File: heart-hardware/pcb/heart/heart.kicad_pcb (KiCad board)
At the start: 4 copper layers, 49.5 x 44 mm, 62 parts, among them J1 3V0, J2 DIO, J3 CLK, J4 GND, SW1 , U1 STM32L031F6Px, U2 TCA6416APWR, U3 LIS3DH

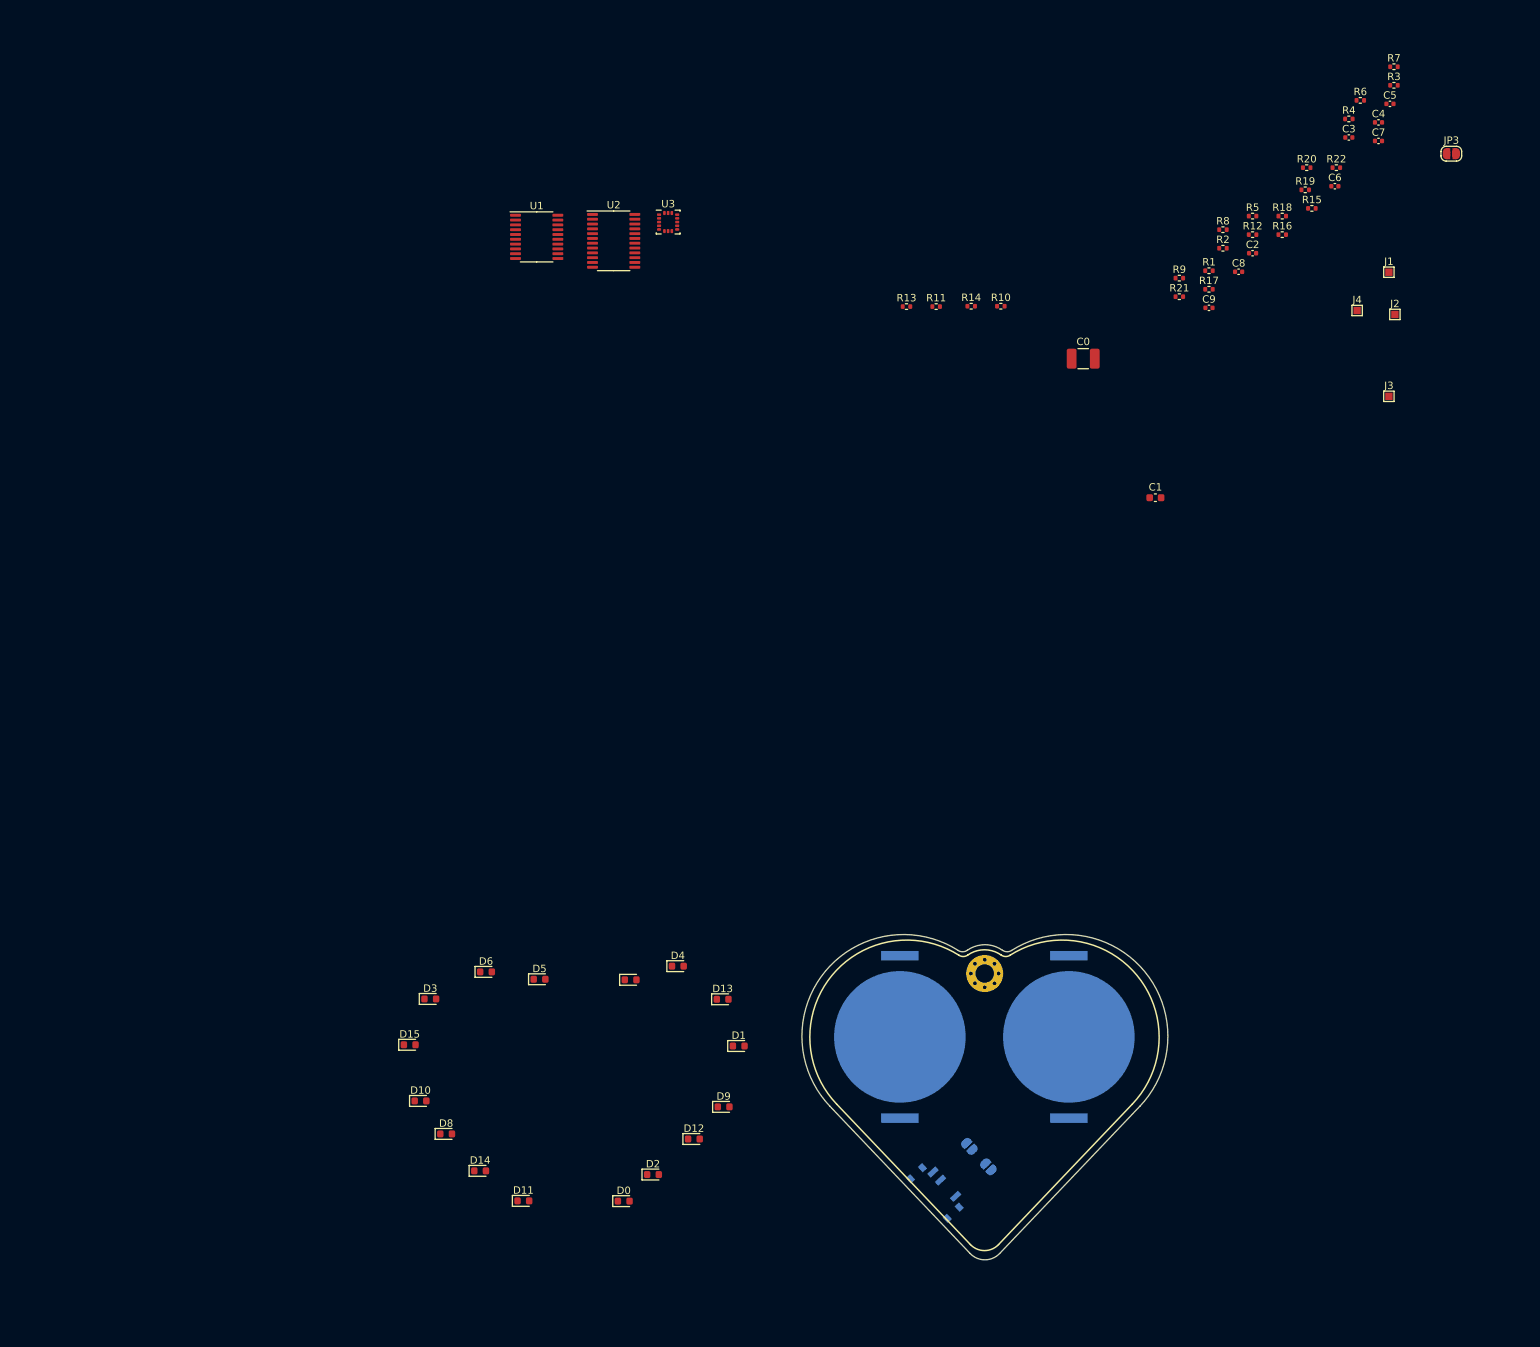
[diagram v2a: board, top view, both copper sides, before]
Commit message: Bottom layer component set
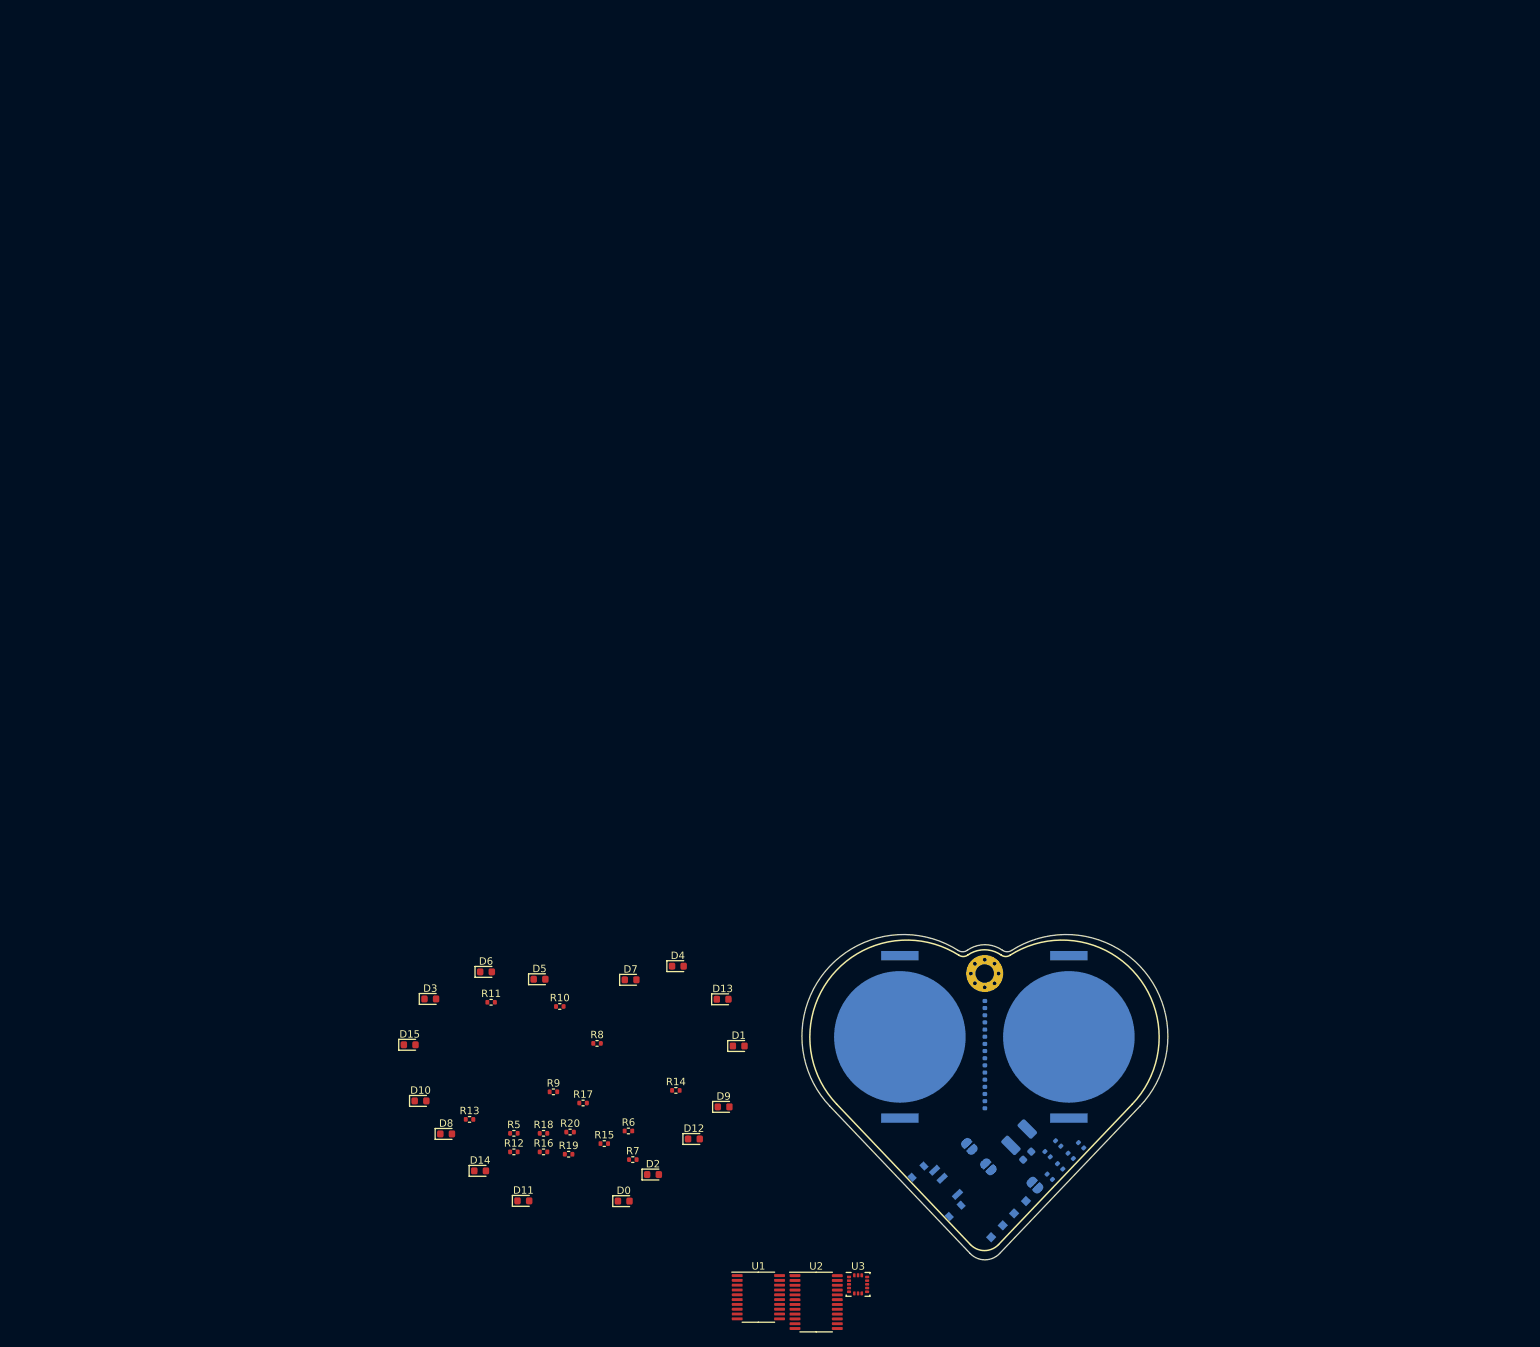
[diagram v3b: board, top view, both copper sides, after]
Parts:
- removed R4: R_Small, Resistor_SMD:R_0402_1005Metric
- added  : , Resistor_SMD:R_0402_1005Metric, B.Cu at (166.2, 145.9)
-  : renamed from C0; value 47uF -> (none); moved to B.Cu
-  : renamed from R3; value 10k -> (none); moved to B.Cu
-  : renamed from R2; value 10k -> (none); moved to B.Cu
-  : renamed from R1; value 10k -> (none); moved to B.Cu
-  : renamed from C9; moved to B.Cu
-  : renamed from C8; moved to B.Cu
-  : renamed from C7; moved to B.Cu
-  : renamed from C6; moved to B.Cu
-  : renamed from C4; moved to B.Cu
-  : renamed from C3; moved to B.Cu
-  : renamed from C2; moved to B.Cu
-  : renamed from C5; moved to B.Cu
-  : renamed from J4; moved to B.Cu
-  : renamed from J3; moved to B.Cu
-  : renamed from J2; moved to B.Cu
-  : renamed from J1; moved to B.Cu
-  : renamed from C1; value 100nF -> (none); moved to B.Cu
-  : renamed from R22; value 10k -> (none); moved to B.Cu
-  : renamed from R21; value 10k -> (none); moved to B.Cu
- RST: renamed from JP3; value Jumper -> (none); moved to B.Cu
- moved R7 180.1 mm to (109.8, 143.6)
- moved R6 171.0 mm to (109.2, 139.7)
- moved R19 164.1 mm to (101.1, 142.9)
- moved R20 164.1 mm to (101.3, 139.9)
- moved R5 159.3 mm to (93.7, 140.0)
- moved R12 159.3 mm to (93.7, 142.6)
- moved R16 159.3 mm to (97.7, 142.6)
- moved R18 159.3 mm to (97.7, 140.0)
- moved R15 158.6 mm to (105.9, 141.4)
- moved   151.3 mm to (169.0, 143.1), turned to 135 degrees
- moved RST 150.4 mm to (164.2, 147.0), turned to 315 degrees
- moved U1 146.5 mm to (126.8, 162.2)
- moved U2 146.1 mm to (134.6, 162.9)
- moved   146.0 mm to (157.4, 136.2), turned to 90 degrees
- moved U3 146.0 mm to (140.3, 160.5)
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
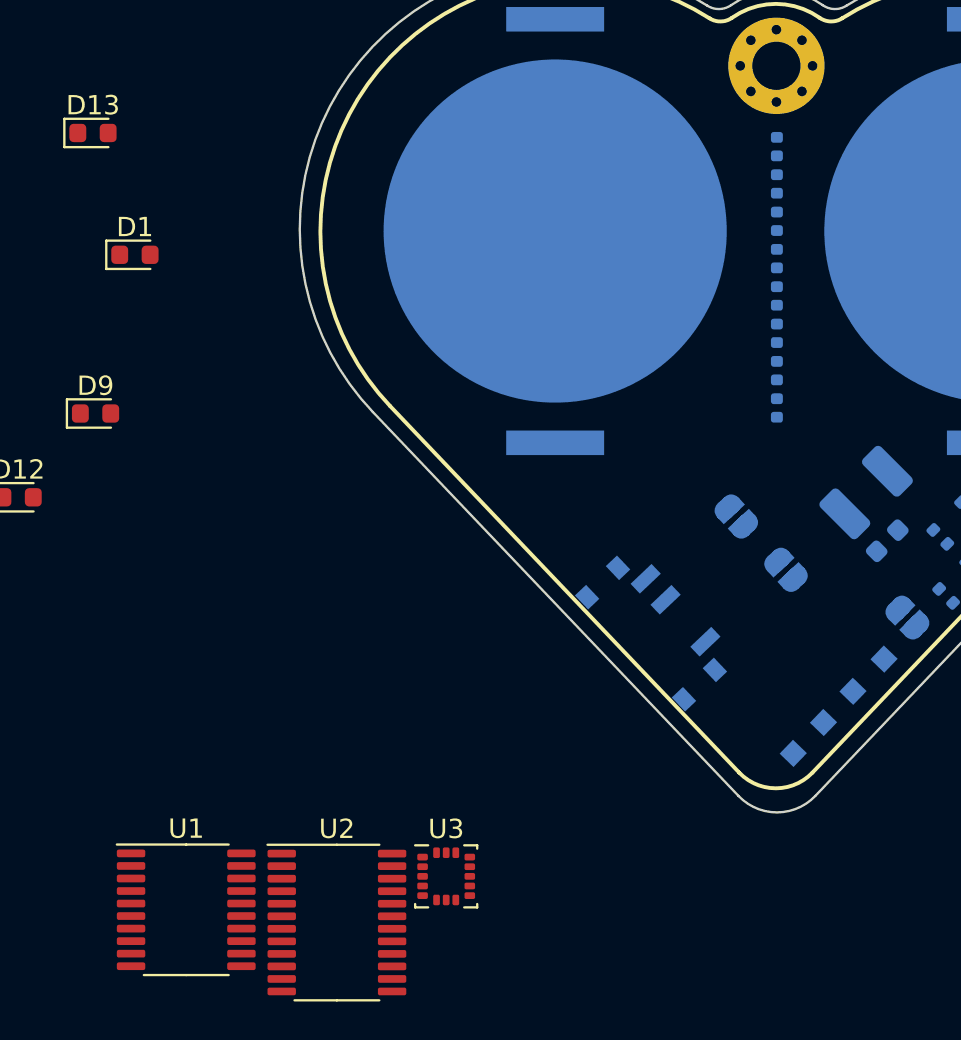
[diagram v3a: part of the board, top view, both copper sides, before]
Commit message: Update heart.kicad_pcb
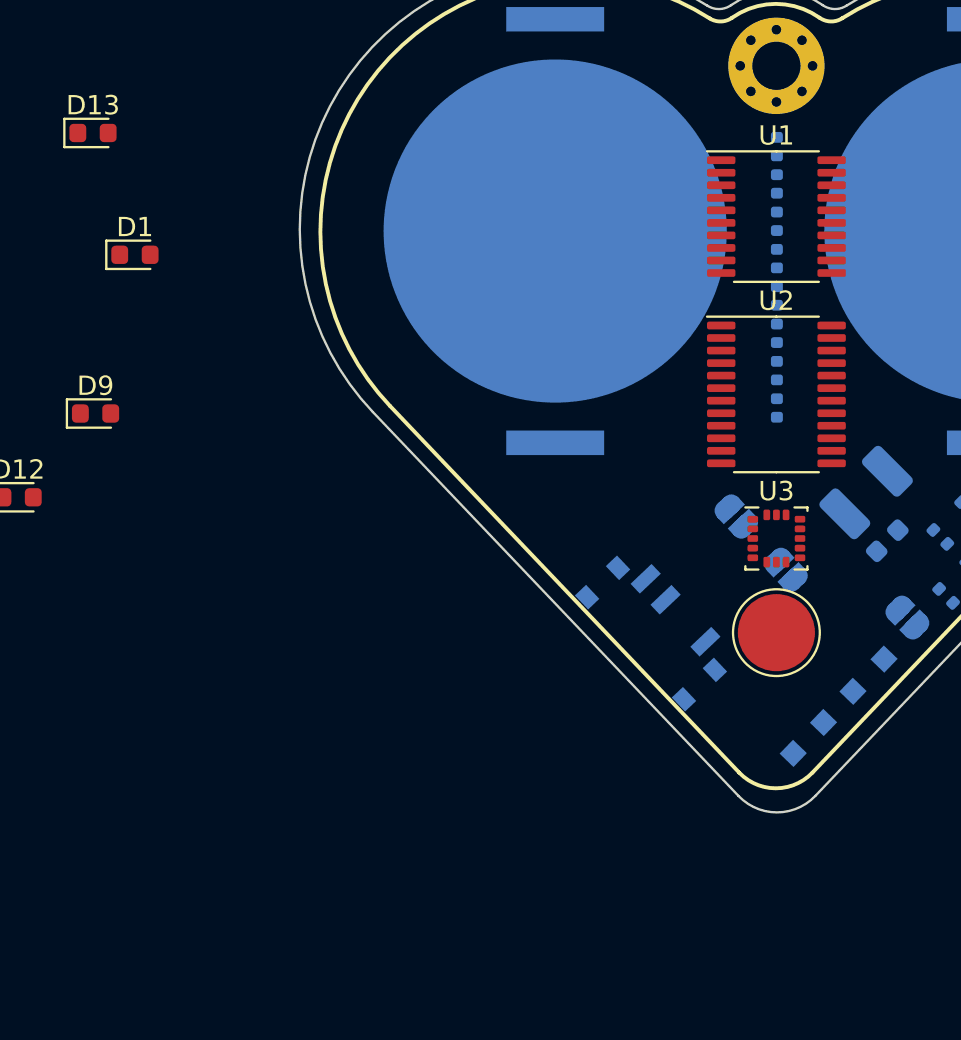
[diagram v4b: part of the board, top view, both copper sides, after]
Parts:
- added  : , TestPoint:TestPoint_Pad_D4.0mm, F.Cu at (157.4, 147.8)
- moved U1 47.2 mm to (157.4, 126.3)
- moved U2 35.6 mm to (157.4, 135.5)
- moved U3 24.5 mm to (157.4, 142.9)
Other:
- board text added: "ADD TOUCH SWITCH!!!!!!"
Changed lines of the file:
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@@
   (general
     (thickness 1.6)
-    (drawings 30)
+    (drawings 31)
     (tracks 0)
     (zones 0)
-    (modules 62)
+    (modules 63)
     (nets 64)
   )
@@
     (34 B.Paste user)
     (35 F.Paste user)
-    (36 B.SilkS user)
+    (36 B.SilkS user hide)
     (37 F.SilkS user)
     (38 B.Mask user)
@@
     (mod_text_size 1 1)
     (mod_text_width 0.15)
-    (pad_size 1.524 1.524)
-    (pad_drill 0.762)
+    (pad_size 4 4)
+    (pad_drill 0)
     (pad_to_mask_clearance 0)
     (aux_axis_origin 0 0)
@@
     (add_net VCC)
   )
+  (module TestPoint:TestPoint_Pad_D4.0mm (layer F.Cu)
+    (at 157.39872 147.83054)
+    (descr "SMD pad as test Point, diameter 4.0mm")
+    (tags "test point SMD pad")
+    (attr virtual)
+    (fp_text reference " " (at 0 -2.898) (layer F.SilkS) hide
+      (effects (font (size 1 1) (thickness 0.15)))
+    )
+    (fp_text value " " (at 0 3.1) (layer F.Fab) hide
+      (effects (font (size 1 1) (thickness 0.15)))
+    )
+    (fp_text user %R (at 0 -2.9) (layer F.Fab)
+      (effects (font (size 1 1) (thickness 0.15)))
+    )
+    (fp_circle (center 0 0) (end 2.5 0) (layer F.CrtYd) (width 0.05))
+    (fp_circle (center 0 0) (end 0 2.25) (layer F.SilkS) (width 0.12))
+    (pad 1 smd circle (at 0 0) (size 4 4) (layers F.Cu))
+  )
   (module Button_Switch_SMD:SW_SPDT_PCM12 (layer B.Cu)
     (at 151.13 147.65274 133.5)
@@
   )
   (module Package_LGA:LGA-16_3x3mm_P0.5mm_LayoutBorder3x5y (layer F.Cu)
-    (at 140.26968 160.47174)
+    (at 157.39872 142.94794)
     (descr "LGA, 16 Pin (http://www.st.com/resource/en/datasheet/lis331hh.pdf), generated with kicad-footprint-generator ipc_noLead_generator.py")
     (tags "LGA NoLead")
@@
   )
   (module Package_SO:TSSOP-24_4.4x7.8mm_P0.65mm (layer F.Cu)
-    (at 134.60222 162.86734)
+    (at 157.39872 135.47432)
     (descr "TSSOP, 24 Pin (JEDEC MO-153 Var AD https://www.jedec.org/document_search?search_api_views_fulltext=MO-153), generated with kicad-footprint-generator ipc_gullwing_generator.py")
     (tags "TSSOP SO")
@@
   )
   (module Package_SO:TSSOP-20_4.4x6.5mm_P0.65mm (layer F.Cu)
-    (at 126.78664 162.20694)
+    (at 157.39872 126.2507)
     (descr "TSSOP, 20 Pin (JEDEC MO-153 Var AC https://www.jedec.org/document_search?search_api_views_fulltext=MO-153), generated with kicad-footprint-generator ipc_gullwing_generator.py")
     (tags "TSSOP SO")
@@
     )
   )
+  (gr_text "ADD TOUCH SWITCH!!!!!!" (at 156.84246 163.54044) (layer Dwgs.User)
+    (effects (font (size 5 5) (thickness 0.3)))
+  )
   (gr_text "OFF\n" (at 155.89504 146.69516 43) (layer B.SilkS)

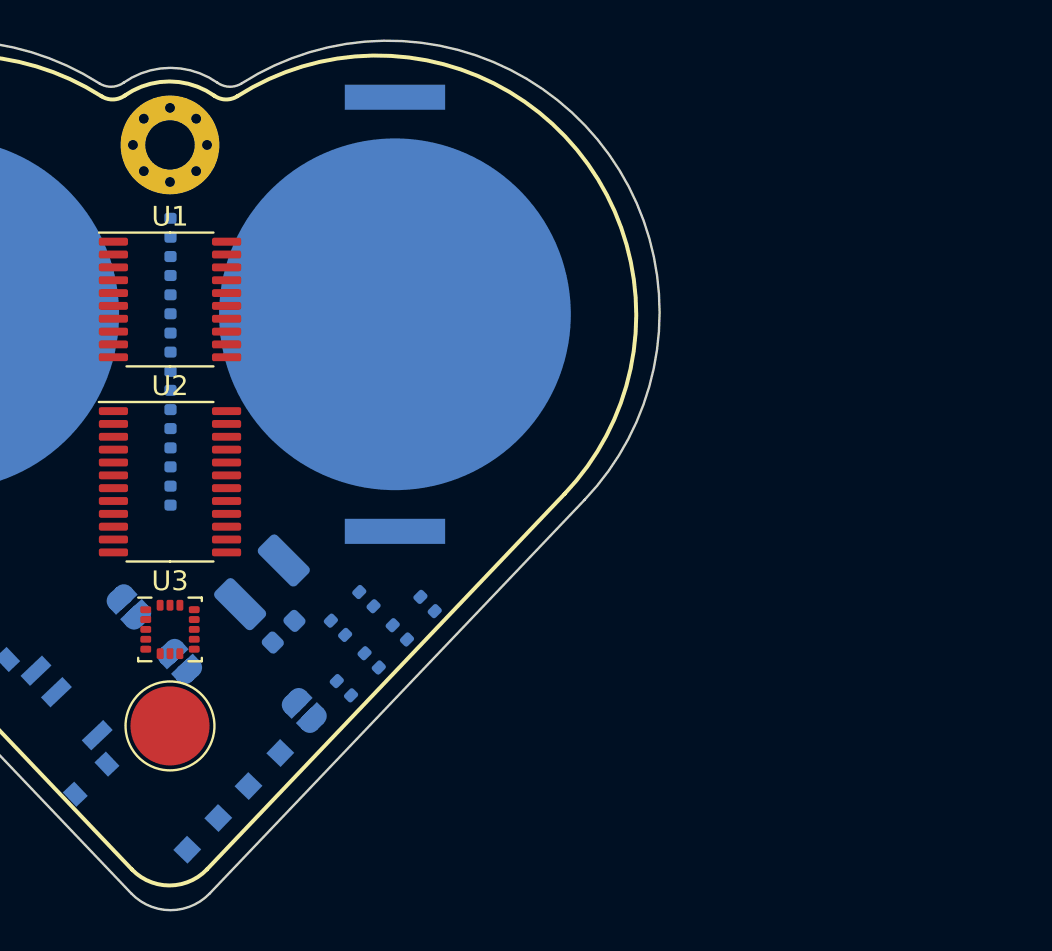
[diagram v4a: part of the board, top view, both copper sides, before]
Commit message: Added touch key
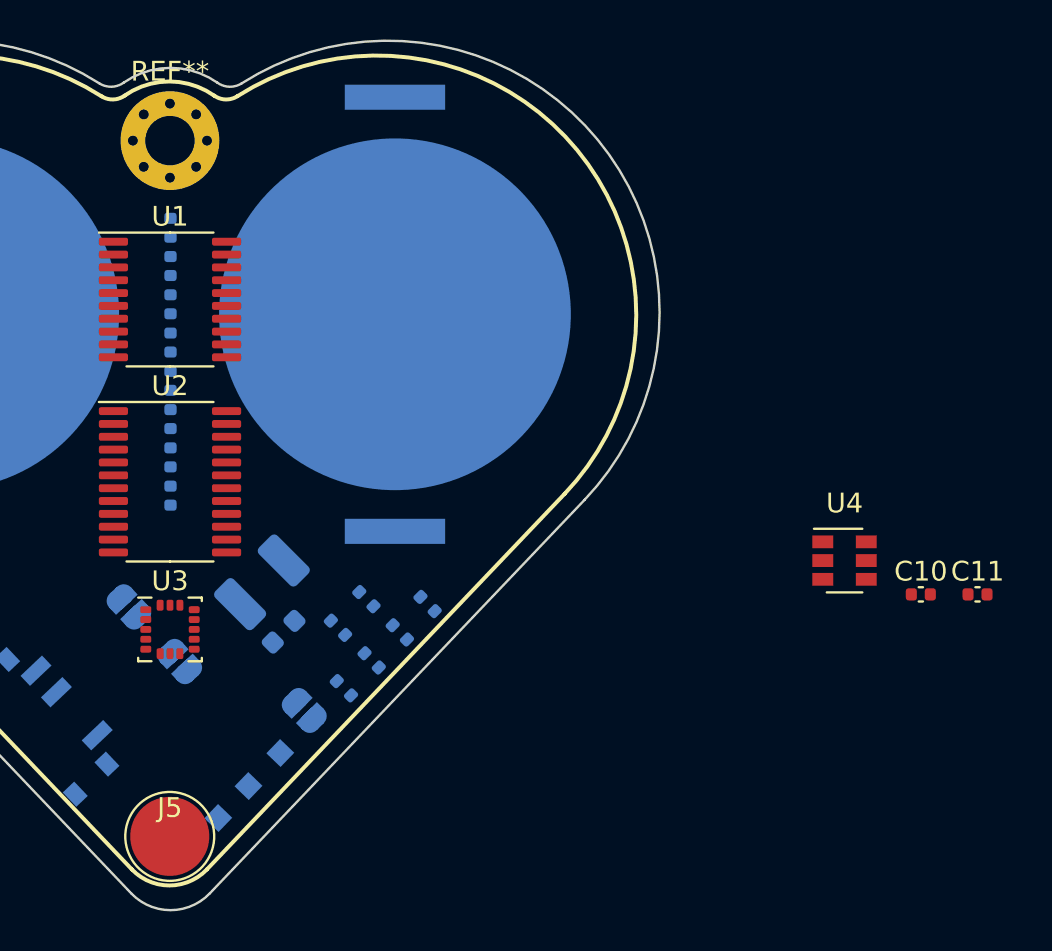
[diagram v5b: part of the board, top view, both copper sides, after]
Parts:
- removed  : , TestPoint:TestPoint_Pad_D4.0mm
- removed  : , MountingHole:MountingHole_2.5mm_Pad_Via
- added C10: 25pF, Capacitor_SMD:C_0402_1005Metric, F.Cu at (195.4, 141.2)
- added C11: 100nF, Capacitor_SMD:C_0402_1005Metric, F.Cu at (198.3, 141.2)
- added J5: TOUCH_KEY, TestPoint:TestPoint_Pad_D4.0mm, F.Cu at (157.4, 153.4)
- added REF**: MountingHole_2.5mm_Pad_Via, MountingHole:MountingHole_2.5mm_Pad_Via, F.Cu at (157.4, 118.2)
- added U4: Holtek-Semicon-BS812A-1, Package_TO_SOT_SMD:SOT-23-6, F.Cu at (191.5, 139.5)
- BT1, BT2, C2, C3, C4, C5, C6, C7, C8, C9, J1, J2, J3, J4, JP1, JP2: renamed from  
- C0: renamed from  ; value (none) -> 47uF
- C1: renamed from  ; value (none) -> 100nF
- JP3: renamed from RST; value (none) -> Jumper
- R1, R2, R21, R22, R3: renamed from  ; value (none) -> 10k
- R4: renamed from  ; value (none) -> R_Small
- SW1: value (none) -> SW_SPDT
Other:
- board text removed: "ADD TOUCH SWITCH!!!!!!"
